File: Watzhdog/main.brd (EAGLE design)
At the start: 100 x 80 mm, 49 parts, among them CN1 MICROUSB(MC-5F-02), IC1 C8051F381-GM, IC3 N25Q512A, IC6 MPU-9250, U1 MCP73831, U2 TPS61201

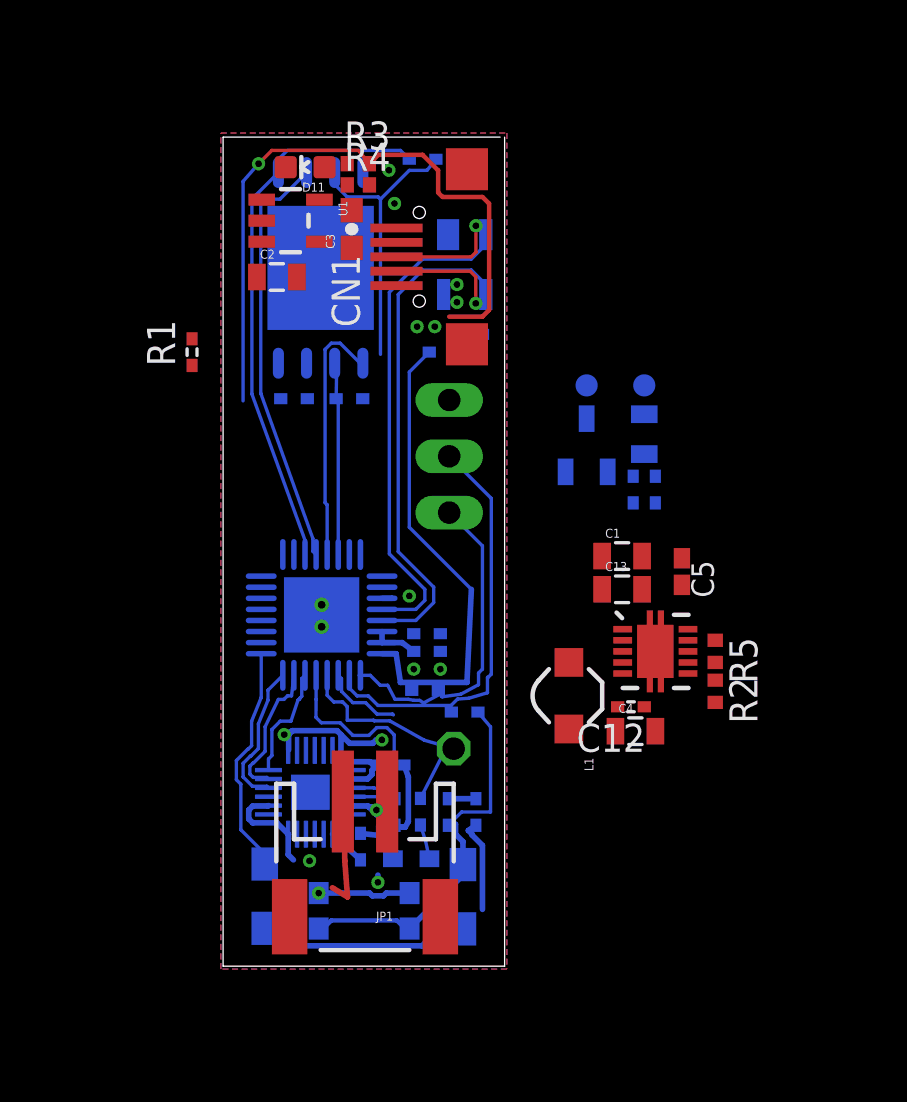
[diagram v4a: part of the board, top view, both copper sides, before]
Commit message: GND 以外の配線概ね終了 PGNDとDGND を接合する準備を開始
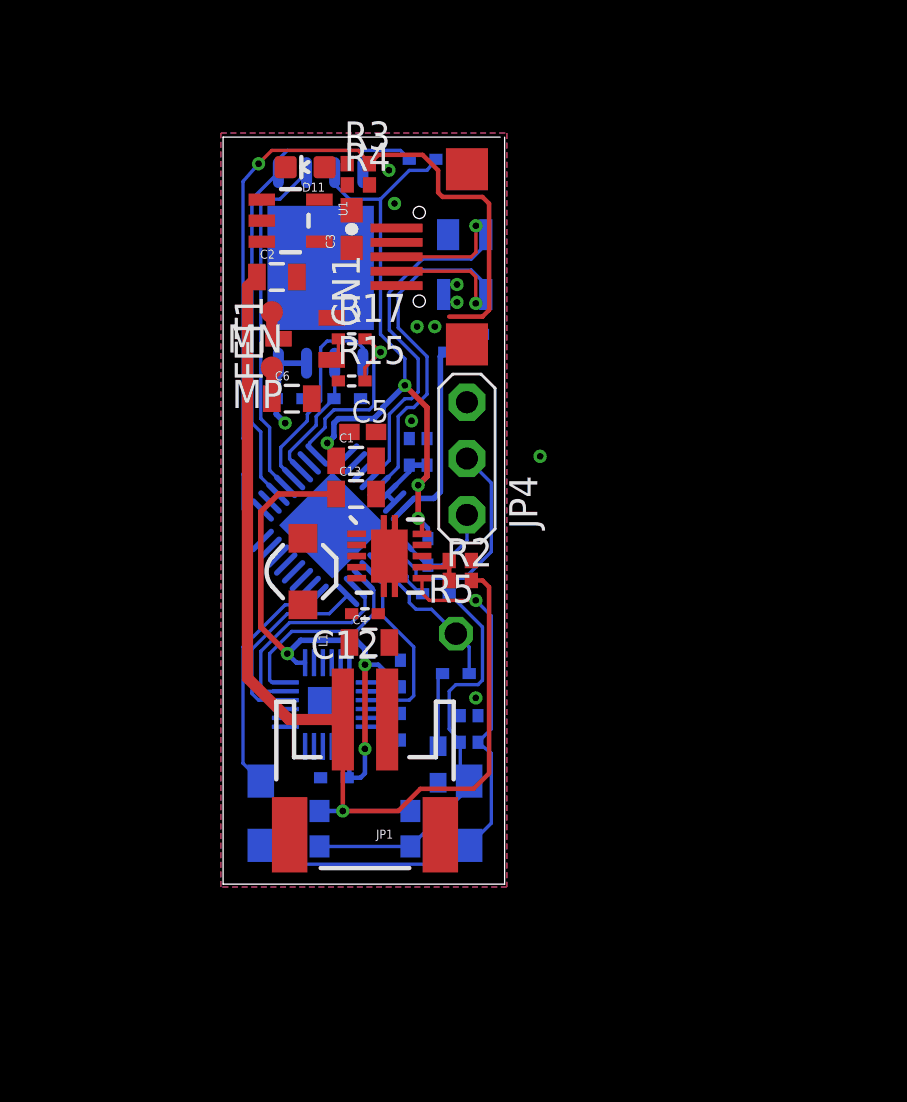
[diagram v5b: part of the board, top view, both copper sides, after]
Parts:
- removed JP3: (no value), pinhead:1X03
- added JP4: 3X1, pin_header:MA3-1
- moved MP 16.8 mm to (53.0, 53.7), flipped to the top, turned to 180 degrees
- moved C6 16.0 mm to (53.9, 52.3), flipped to the top, turned to 0 degrees
- moved C5 15.7 mm to (57.1, 50.8), turned to 0 degrees
- moved MN 14.6 mm to (53.0, 56.2), flipped to the top, turned to 180 degrees
- moved R15 14.5 mm to (56.6, 53.1), flipped to the top, turned to 0 degrees
- moved R17 14.4 mm to (56.6, 55.0), flipped to the top, turned to 0 degrees
- moved FET1 13.6 mm to (54.5, 55.0), flipped to the top, turned to 90 degrees
- moved L1 13.2 mm to (54.4, 44.5)
- moved U2 12.7 mm to (58.3, 45.2)
- moved C1 12.7 mm to (56.8, 49.5)
- moved C13 12.7 mm to (56.8, 48.0)
- moved C12 12.7 mm to (57.2, 42.6)
- moved C4 12.6 mm to (57.4, 41.3)
- moved R2 12.5 mm to (61.5, 44.1), turned to 0 degrees
- moved R5 12.2 mm to (61.5, 45.0), turned to 180 degrees
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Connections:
- net C2CK: now also JP4.1; no longer JP3.3
- net C2D: now also JP4.2; no longer JP3.2
- net DGND2: now also JP4.3; no longer JP3.1
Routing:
- net VDD_BATT: track 9.34 -> 50.3 mm
- net +3V3: track 27.7 -> 65.4 mm, vias 4 -> 8
- net DGND2: track 18.7 -> 0.00 mm, vias 7 -> 5
- net N$18: track 21.4 -> 8.43 mm
- net PWR_EN: track 13.8 -> 25.6 mm, vias 0 -> 1
- net C2CK: track 14.9 -> 4.99 mm
- net PWM: track 0.00 -> 9.58 mm, vias 0 -> 1
- net C2D: track 18.9 -> 10.9 mm
- net D-: track 27.2 -> 20.3 mm
- net D+: track 27.2 -> 20.5 mm
- net IMU_MOSI: track 5.17 -> 9.13 mm
- net N$15: track 10.5 -> 7.04 mm
- net IMU_SCK: track 6.33 -> 9.44 mm
- net EEPROM_MISO: track 18.9 -> 15.9 mm
- net EEPROM_SCK: track 8.70 -> 5.91 mm
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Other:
- outline, holes or cut-outs redrawn

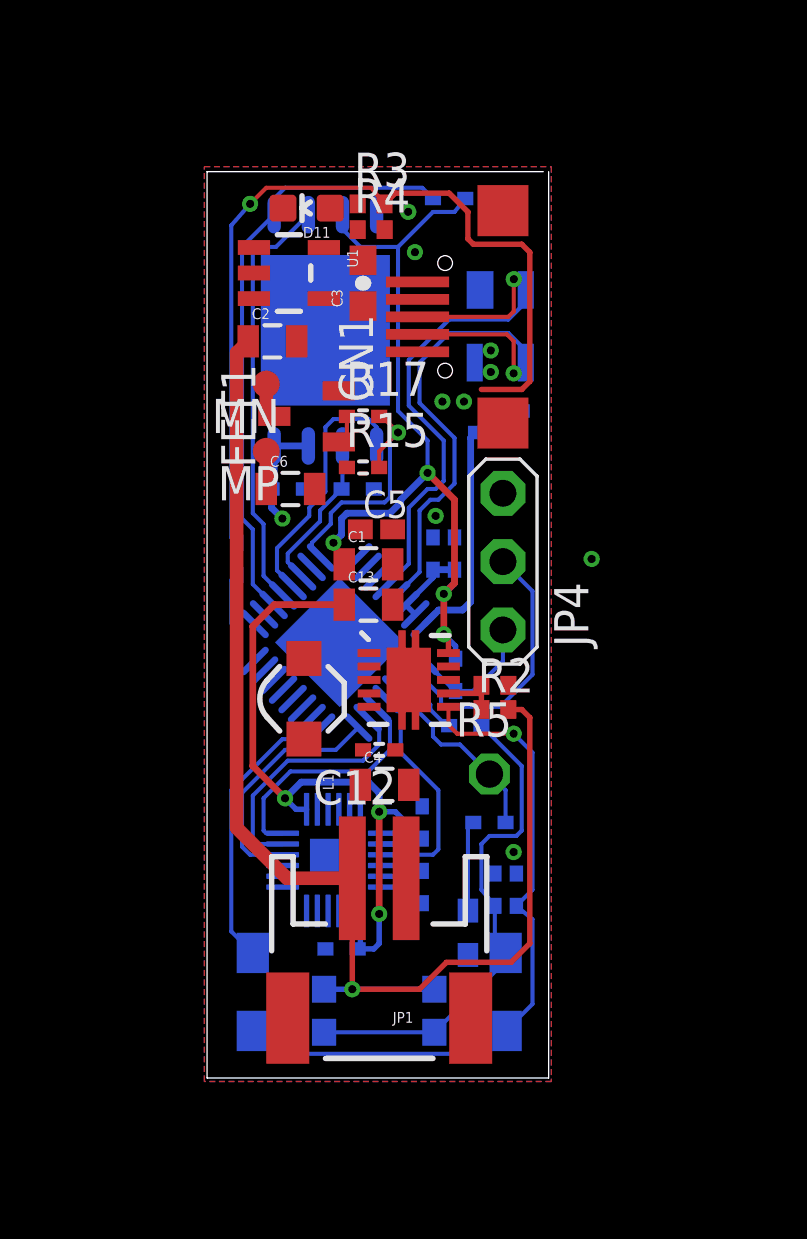
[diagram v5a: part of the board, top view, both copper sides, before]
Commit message: PGND，DGND 以外の配線，ポリゴン貼り完了
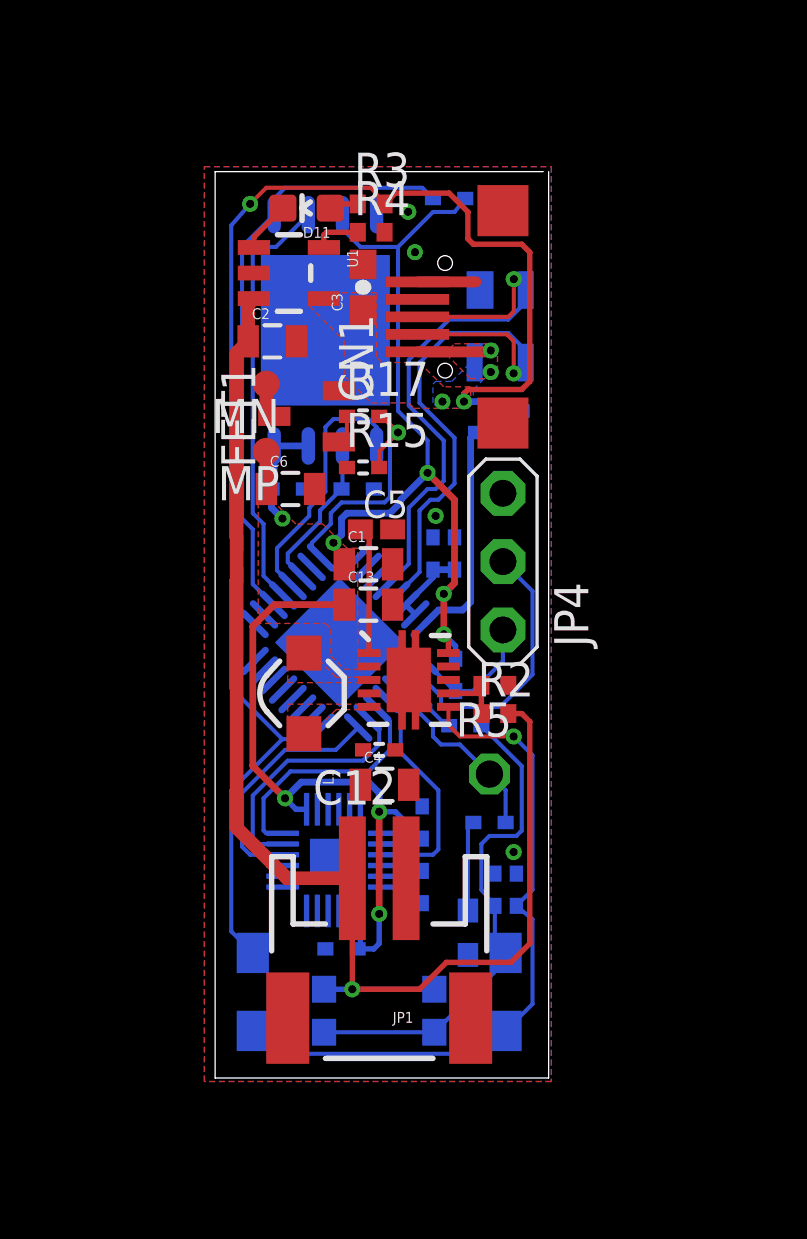
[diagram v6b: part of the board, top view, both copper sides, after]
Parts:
- moved L1 0.20 mm to (54.4, 44.7)
- moved C3 0.15 mm to (56.6, 59.8)
- moved R2 0.15 mm to (61.5, 44.0)
- moved R4 0.10 mm to (56.9, 61.8)
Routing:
- net VBUS: track 32.4 -> 38.3 mm
- net PWR_EN_2: track 12.6 -> 17.7 mm
- net VAUX: track 0.00 -> 4.73 mm
- net DGND2: track 0.00 -> 2.17 mm, vias 5 -> 4
- net STAT: track 0.00 -> 1.91 mm
- net PROG: track 0.00 -> 1.76 mm
- net VDD_BATT: track 50.3 -> 51.8 mm
- net N$3: track 0.00 -> 1.09 mm
- added copper zone on layer 1, net +3V3
- added copper zone on layer 1, net LIN
- added copper zone on layer 1, net VBUS
- added copper zone on layer 16, net VBUS
- added copper zone on layer 1, net VDD_BATT
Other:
- outline, holes or cut-outs redrawn

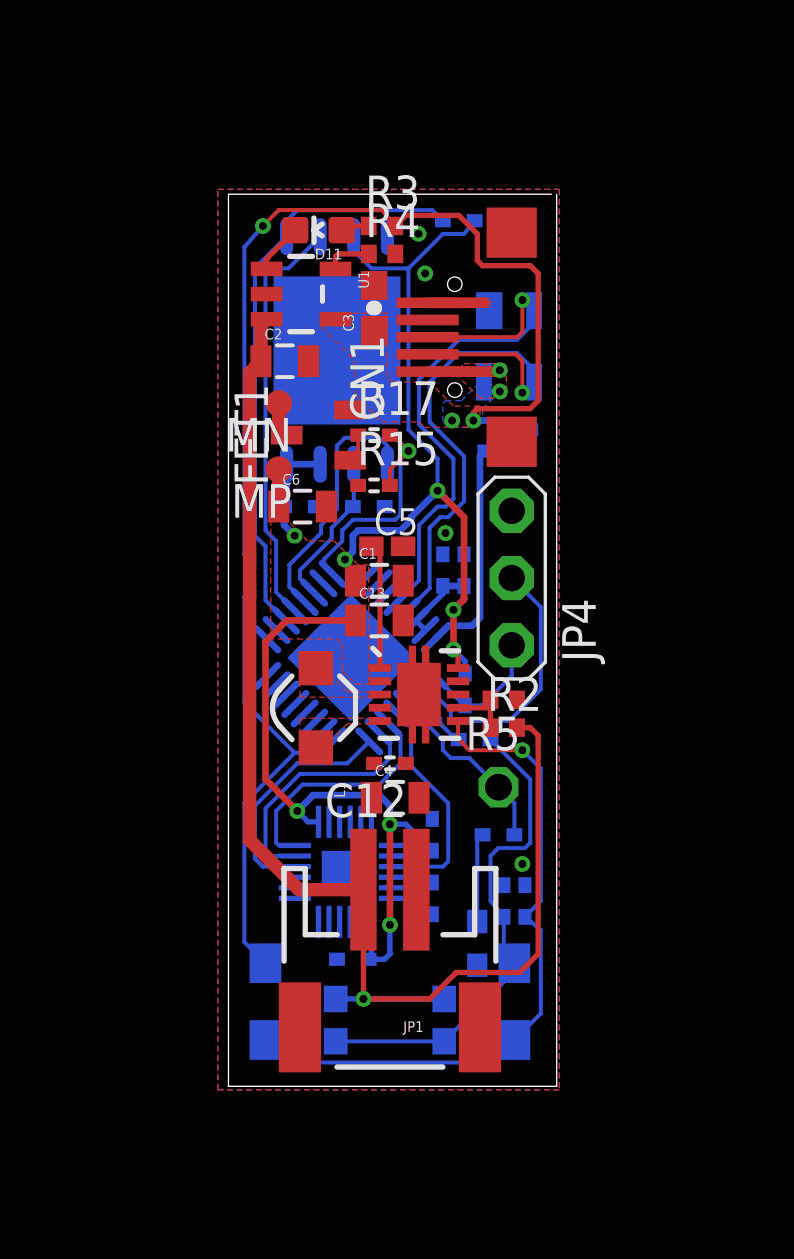
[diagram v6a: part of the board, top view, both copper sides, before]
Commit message: airwire 0 本 GND 含めポリゴン貼り完了
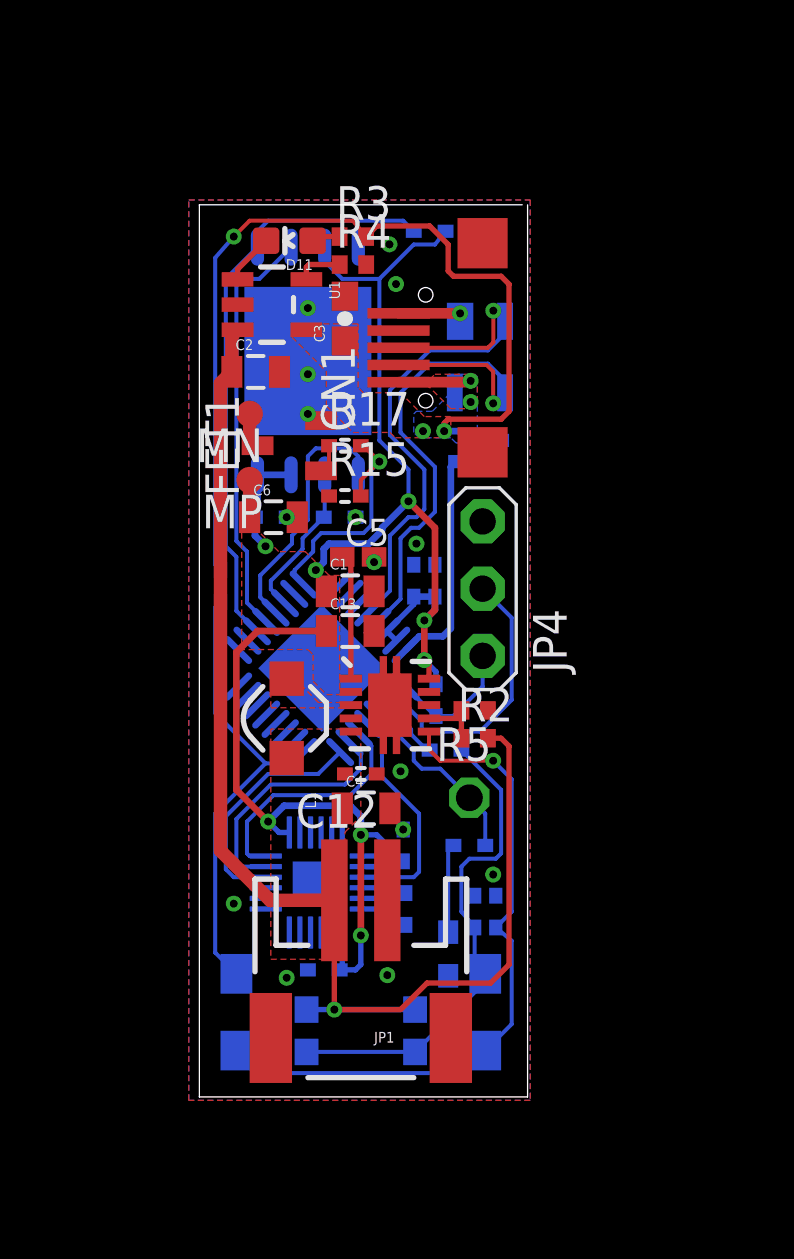
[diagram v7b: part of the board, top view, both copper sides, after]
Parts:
- moved CN1 1.17 mm to (57.4, 58.3)
- moved IC3 1.17 mm to (54.1, 57.8)
- moved L1 1.17 mm to (53.3, 44.3)
- moved MN 1.17 mm to (51.9, 55.8)
- moved MP 1.17 mm to (51.9, 53.3)
- moved R1 1.17 mm to (50.8, 49.3)
- moved R12 1.17 mm to (60.8, 54.8)
- moved R2 1.17 mm to (60.4, 43.5)
- moved U1 1.17 mm to (52.7, 59.9)
- moved C10 1.17 mm to (58.1, 49.5)
- moved C12 1.17 mm to (56.1, 42.2)
- moved C14 1.17 mm to (58.9, 49.5)
- moved C2 1.17 mm to (52.1, 57.4)
- moved C3 1.17 mm to (55.5, 59.4)
- moved C4 1.17 mm to (56.3, 40.9)
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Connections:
- removed net DGND2: C10.P$1, C11.P$1, C14.P$1, C2.2, C3.2, C5.2, C6.2, C7.P$1, C8.P$1, C9.P$1, CN1.5, D3.1, FET1.S, IC1.3, IC1.B, IC3.4, IC3.B, IC6.11, IC6.18, IC6.20, JP1.1, JP4.3, LED1.K, R12.P$1, R13.P$1, R14.P$1, R15.P$1, R26.P$1, R4.2, R5.1, U1.2, U2.8, U2.9
- removed net PGND: C1.2, C12.P$1, C13.2, C4.2, U2.11, U2.12, U2.13, U2.14, U2.15, U2.4
- new net DGND: C1.2, C10.P$1, C11.P$1, C12.P$1, C13.2, C14.P$1, C2.2, C3.2, C4.2, C5.2, C6.2, C7.P$1, C8.P$1, C9.P$1, CN1.5, D3.1, FET1.S, IC1.3, IC1.B, IC3.4, IC3.B, IC6.11, IC6.18, IC6.20, JP1.1, JP4.3, LED1.K, R12.P$1, R13.P$1, R14.P$1, R15.P$1, R26.P$1, R4.2, R5.1, U1.2, U2.11, U2.12, U2.13, U2.14, U2.15, U2.4, U2.8, U2.9
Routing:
- net DGND: track 0.00 -> 2.18 mm, vias 0 -> 16
- net DGND2: track 2.17 -> 0.00 mm, vias 4 -> 0
- net D-: track 20.3 -> 20.9 mm
- net D+: track 20.5 -> 21.2 mm
- added copper zone on layer 1, net DGND
- added copper zone on layer 16, net DGND
- removed copper zone on layer 1, net DGND2
- removed copper zone on layer 16, net DGND2
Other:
- outline, holes or cut-outs redrawn
